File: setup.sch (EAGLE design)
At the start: 92 parts, among them K2 CPC1708J, K4 LY30, K5 CPC1708J, K6 LY30

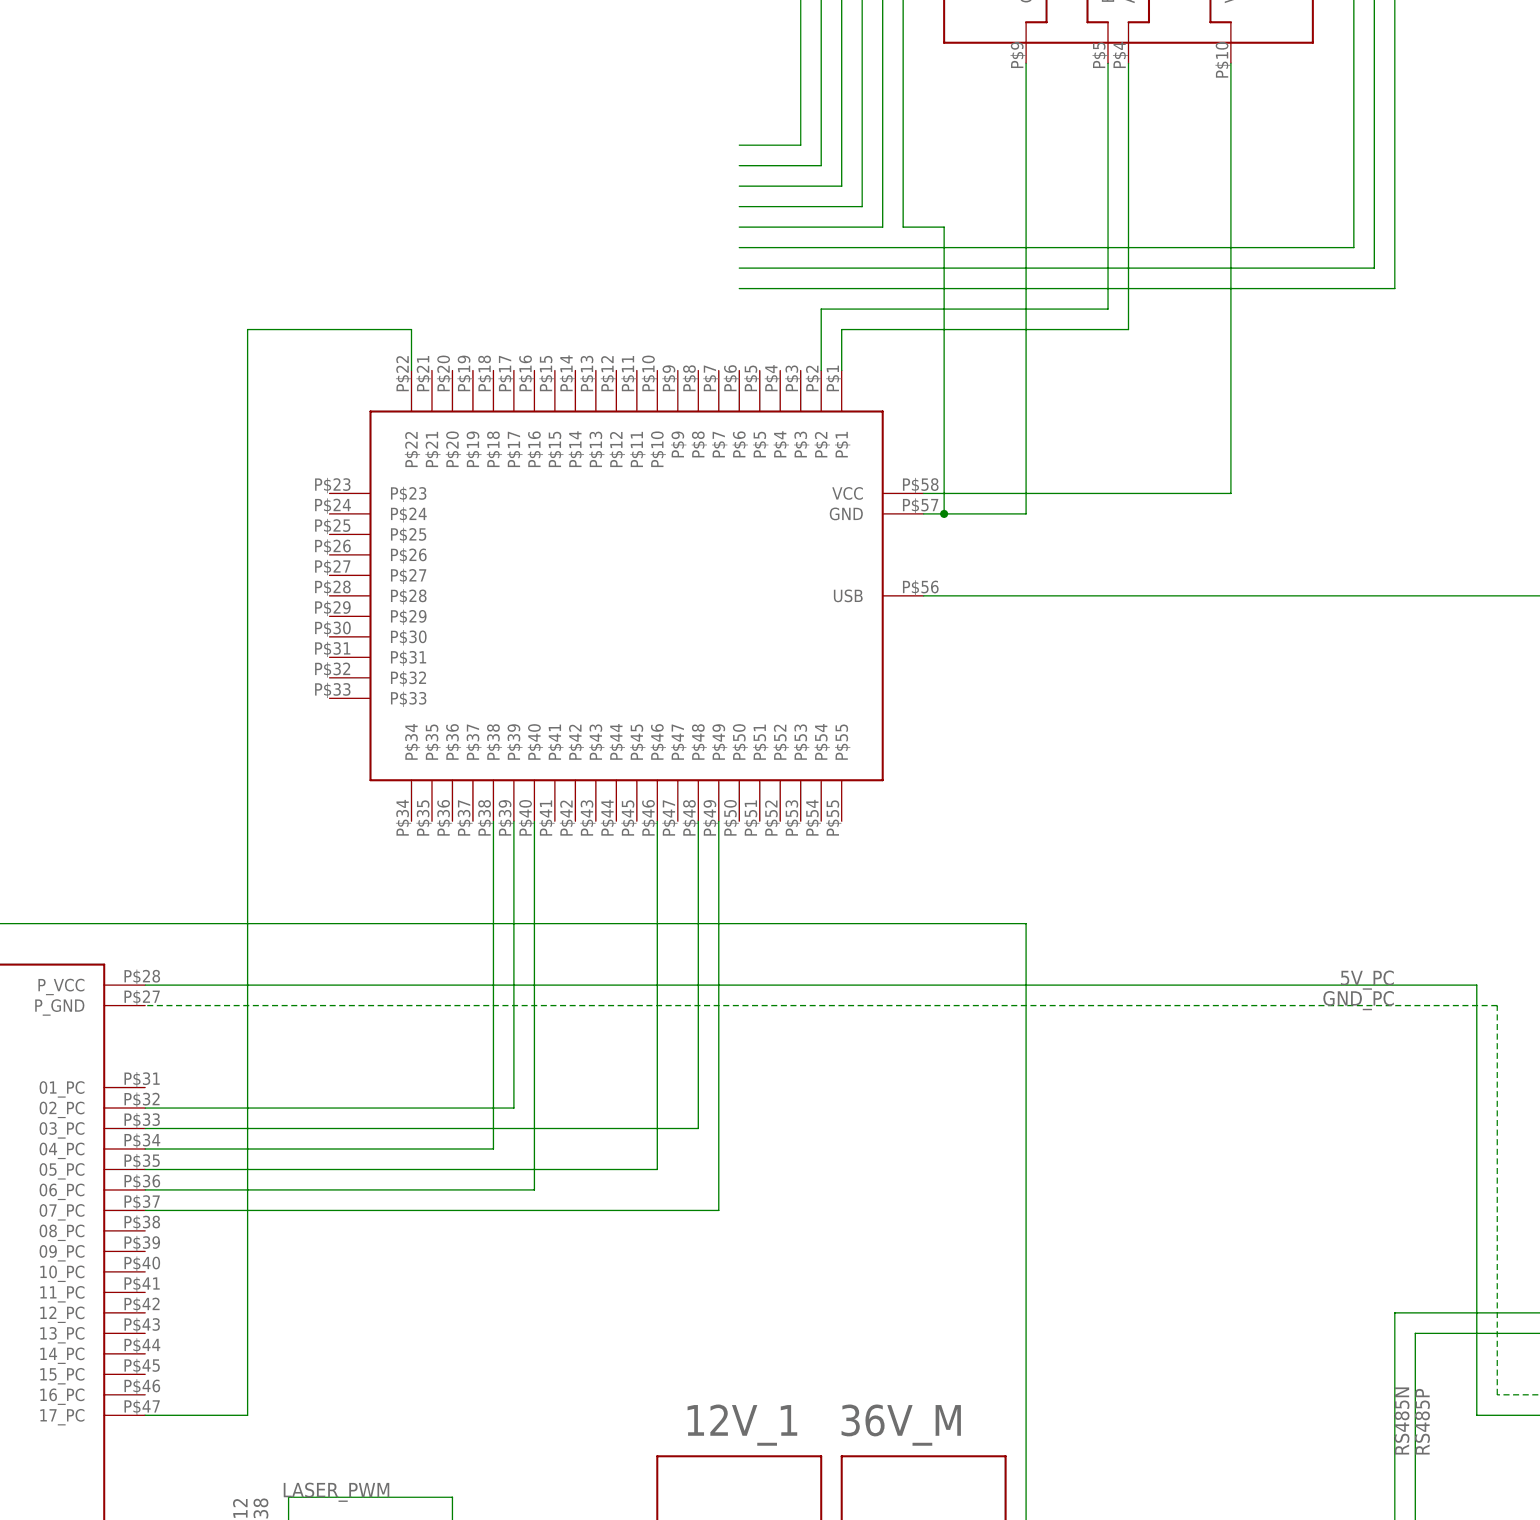
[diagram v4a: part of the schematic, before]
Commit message: connected pendant
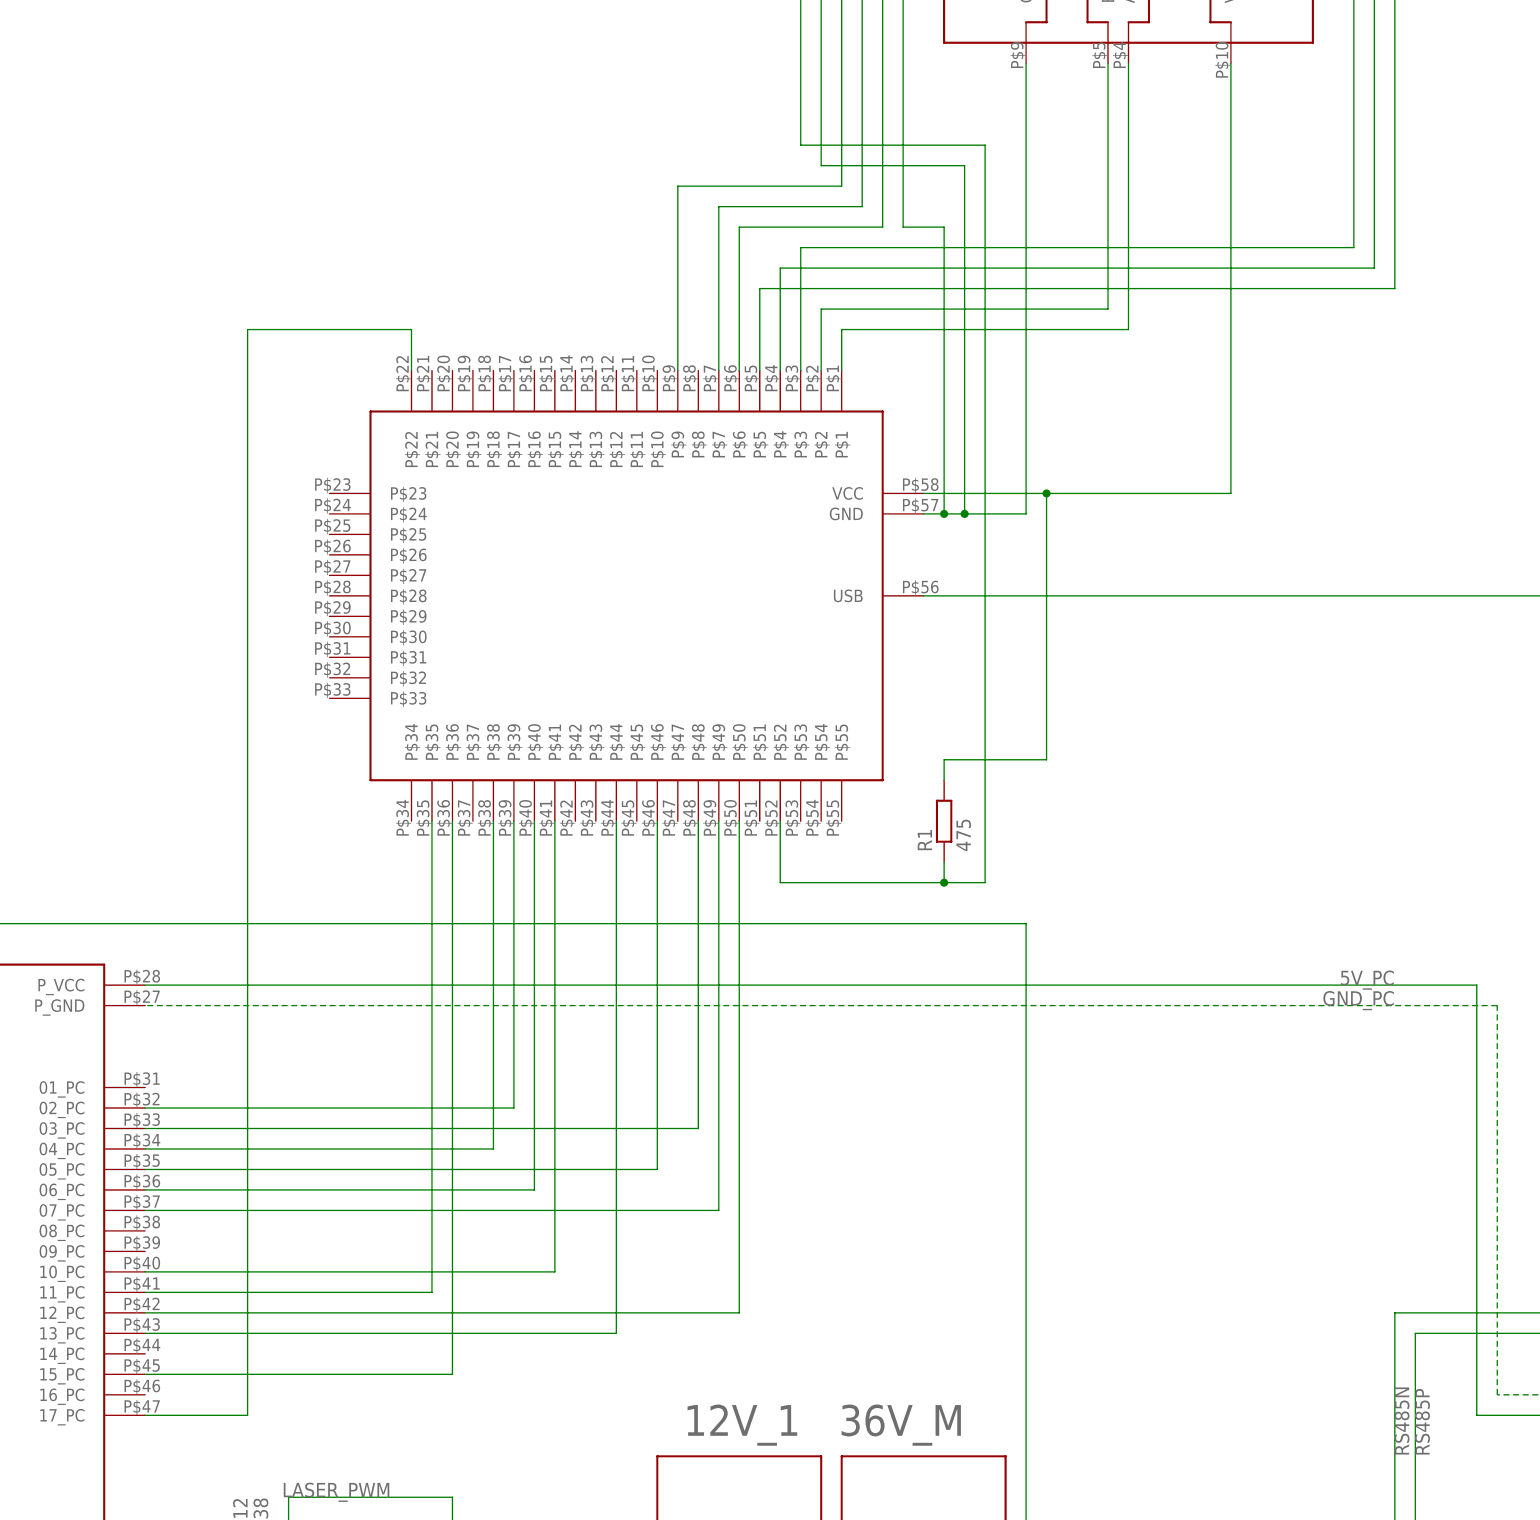
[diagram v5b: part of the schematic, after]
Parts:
- added R1: 475, rcl:R-EU_0204/2V
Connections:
- removed net N$67: U$13.C
- new net N$17: U$1.10_PC, U$4.P$41
- new net N$58: U$1.11_PC, U$4.P$35
- new net N$59: U$1.12_PC, U$4.P$50
- new net N$60: U$1.13_PC, U$4.P$44
- new net N$61: U$1.15_PC, U$4.P$36
- net N$48: now also U$13.C
- net N$51: now also R1.2
- net N$54: now also U$4.P$5
- net N$55: now also U$4.P$4
- net N$56: now also U$4.P$3
- net N$64: now also U$4.P$6
- net N$65: now also U$4.P$7
- net N$66: now also U$4.P$9
- net N$68: now also R1.1, U$4.P$52
